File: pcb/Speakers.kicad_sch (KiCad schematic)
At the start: 34 parts, among them U4 ADA4891, U7 ADA4891

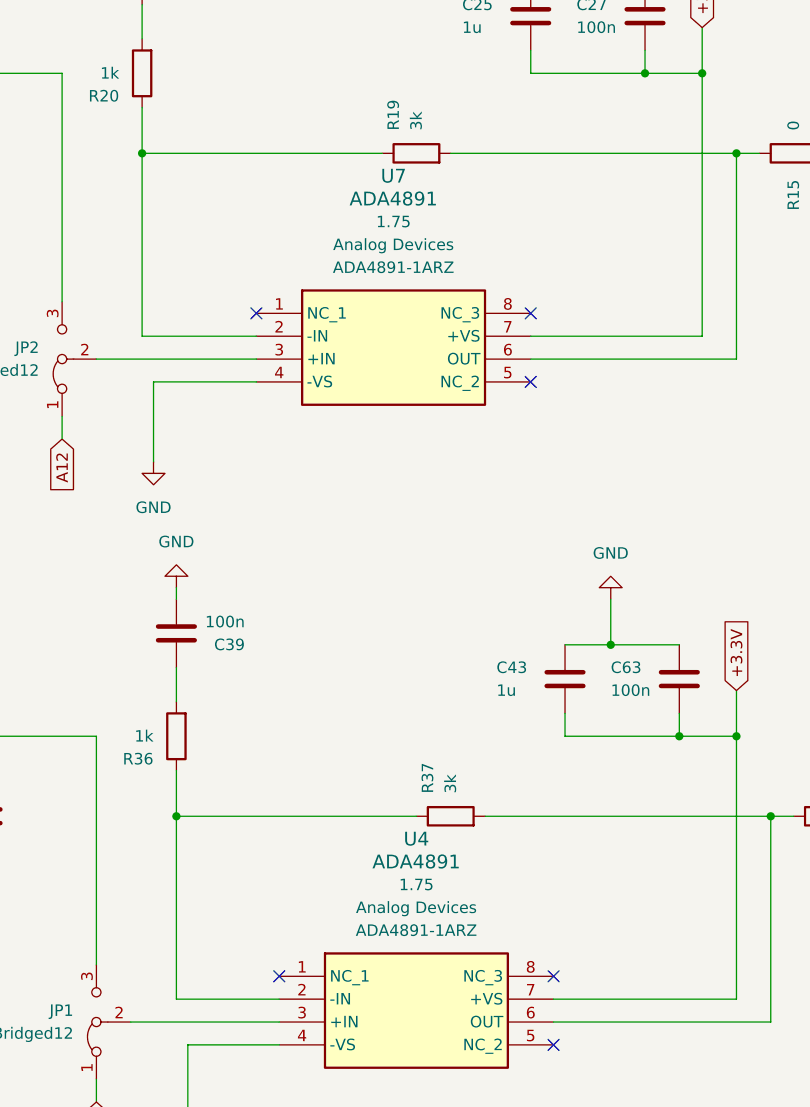
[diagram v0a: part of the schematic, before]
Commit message: feat: PCB Cleanup and Reorganization
Fixing Project Library Structure
Footprint library
Symbol library
3D Models
Component Datasheets
ERC and DRC error and warning fixes
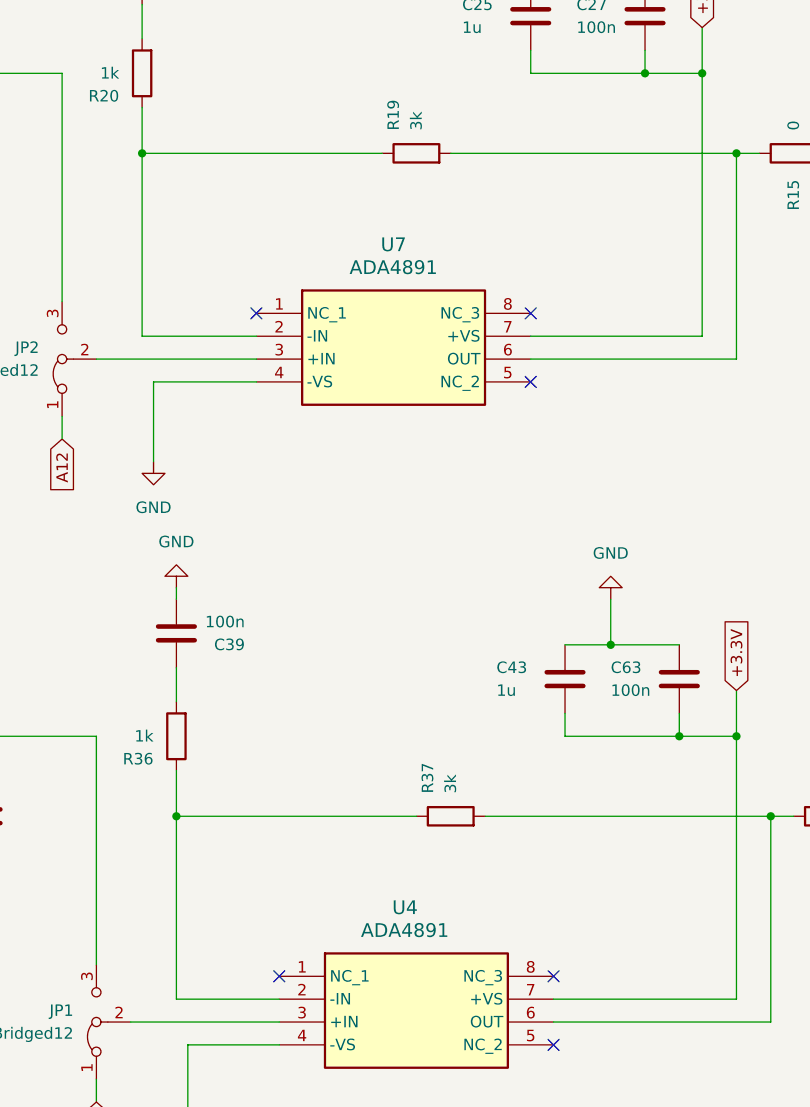
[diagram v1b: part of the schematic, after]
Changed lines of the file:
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@@
 		(on_board yes)
 		(dnp no)
-		(fields_autoplaced yes)
 		(property "Reference" "U7"
-			(at 118.11 50.8 0)
+			(at 118.11 58.42 0)
 			(effects
 				(font
@@
 		)
 		(property "Value" "ADA4891"
-			(at 118.11 53.34 0)
+			(at 118.11 60.96 0)
 			(effects
 				(font
@@
 					(size 1.27 1.27)
 				)
+				(hide yes)
 			)
 		)
@@
 					(size 1.27 1.27)
 				)
+				(hide yes)
 			)
 		)
@@
 					(size 1.27 1.27)
 				)
+				(hide yes)
 			)
 		)
@@
 		(on_board yes)
 		(dnp no)
-		(fields_autoplaced yes)
 		(property "Reference" "U4"
-			(at 120.65 124.46 0)
+			(at 119.38 132.08 0)
 			(effects
 				(font
@@
 		)
 		(property "Value" "ADA4891"
-			(at 120.65 127 0)
+			(at 119.38 134.62 0)
 			(effects
 				(font
@@
 					(size 1.27 1.27)
 				)
+				(hide yes)
 			)
 		)
@@
 					(size 1.27 1.27)
 				)
+				(hide yes)
 			)
 		)
@@
 					(size 1.27 1.27)
 				)
-			)
-		)
+				(hide yes)
+			)
+		)

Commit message: Polishin pt1
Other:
- company: (none) -> Infineon Technologies
- title: (none) -> SensEdu 0.7
- moved on the sheet: C21, C22, C23, C24, C25, C26, C27, C32, C34, C35, C39, C43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

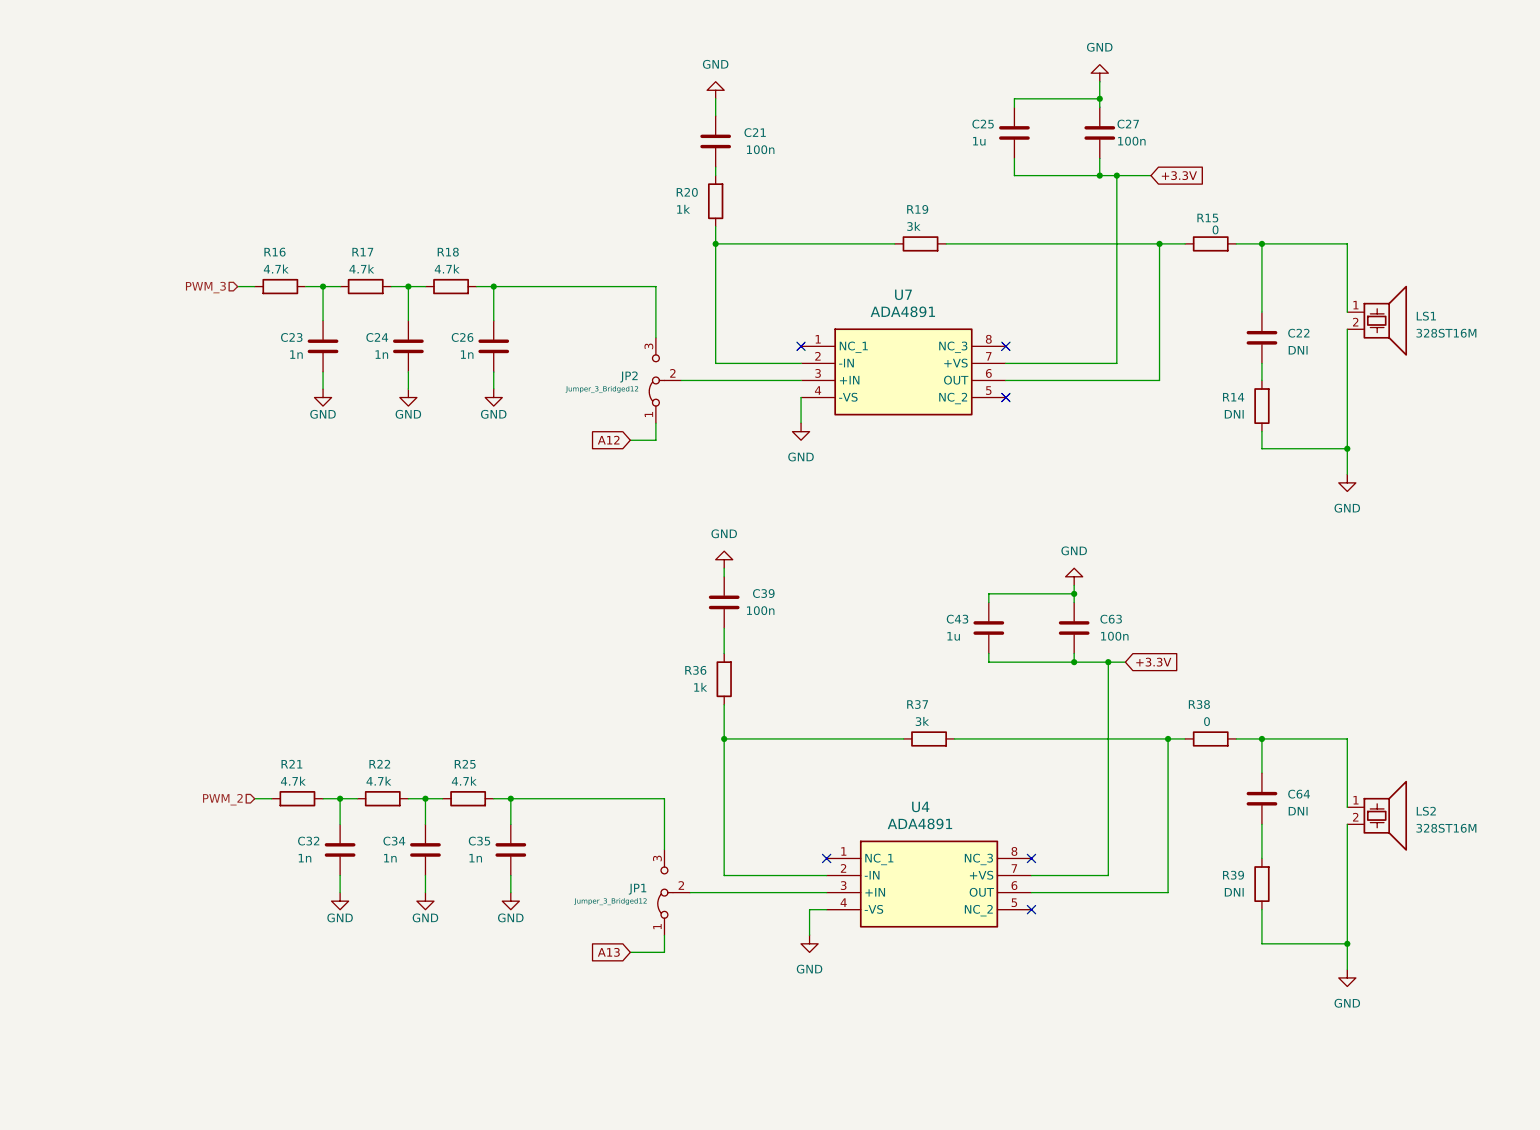
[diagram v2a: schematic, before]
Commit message: refactor: Edit speaker/mic symbols and polish
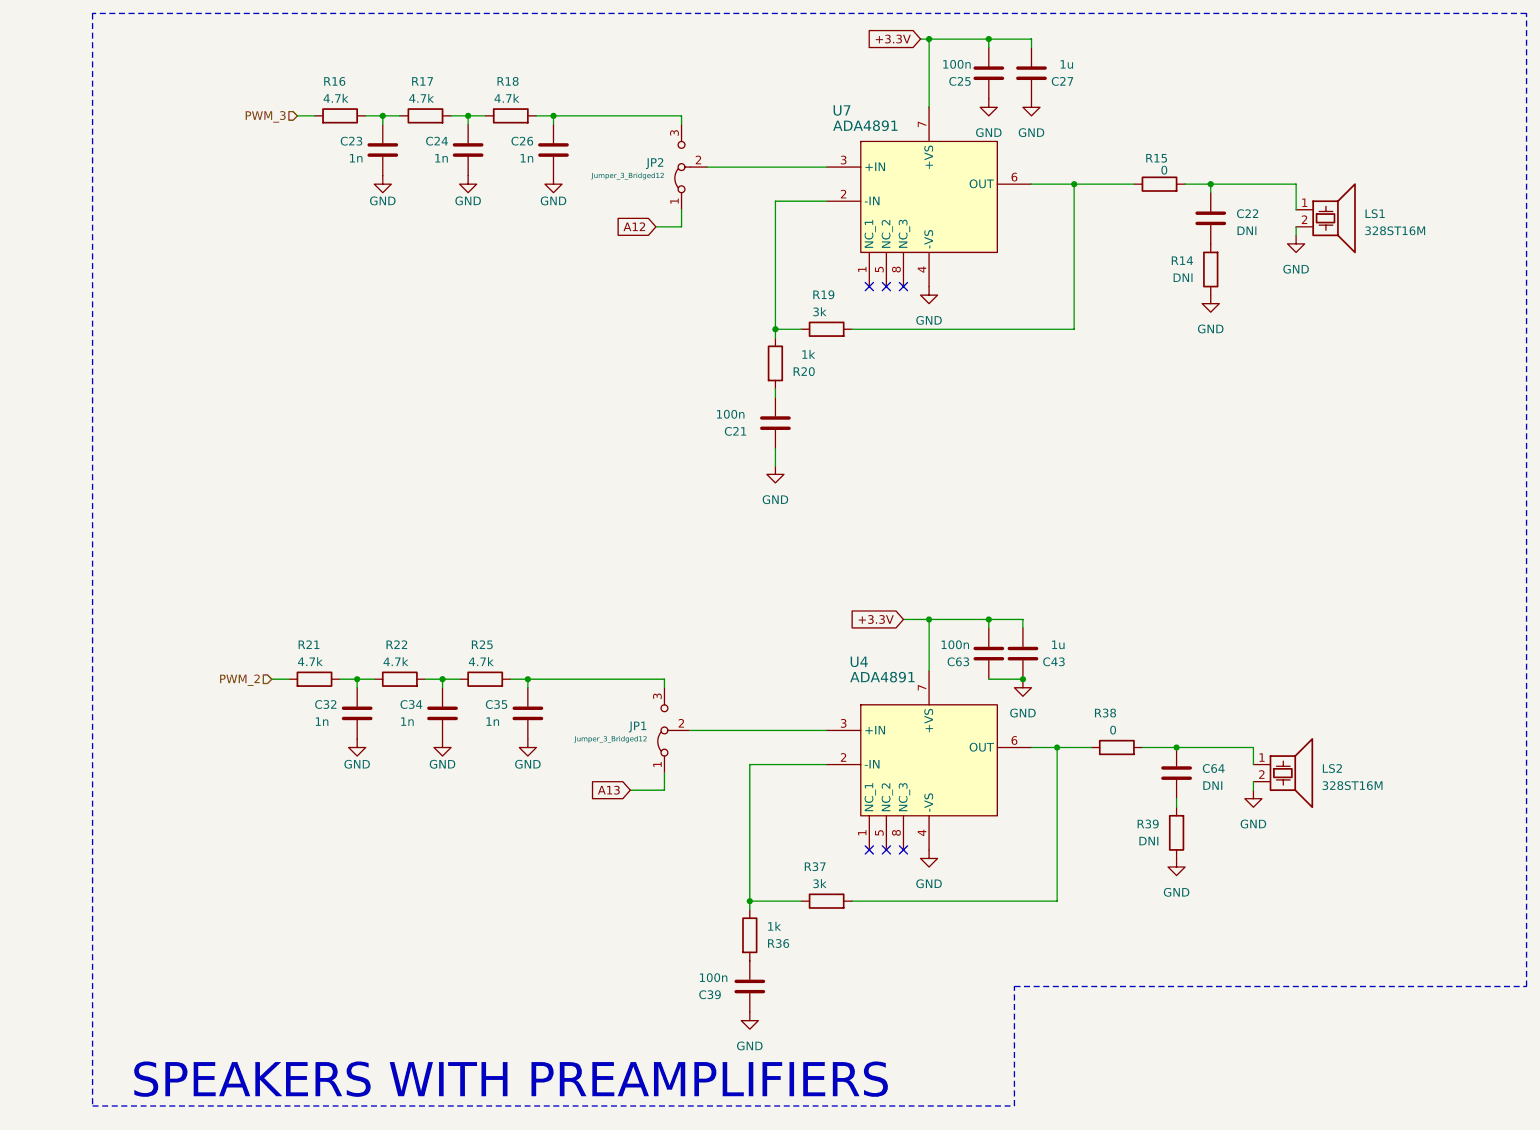
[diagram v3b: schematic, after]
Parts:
- C25: value 1u -> 100n
- C27: value 100n -> 1u
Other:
- note added: "SPEAKERS WITH PREAMPLIFIERS"
- moved on the sheet: C22, C23, C24, C26, C32, C34, C35, C43, C63, C64, JP1, JP2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
